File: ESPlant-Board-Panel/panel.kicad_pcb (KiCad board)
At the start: 2 copper layers, 156 x 147 mm, 408 parts, among them J1 Conn_01x05, U1 ESP32-C6-MINI-1/U, U3 Reset, U4 Boot, U5 Temp/Humid-Sensor, U6 Light sensor, U7 AMS1117-3_3, U8 MK-12C02-G025

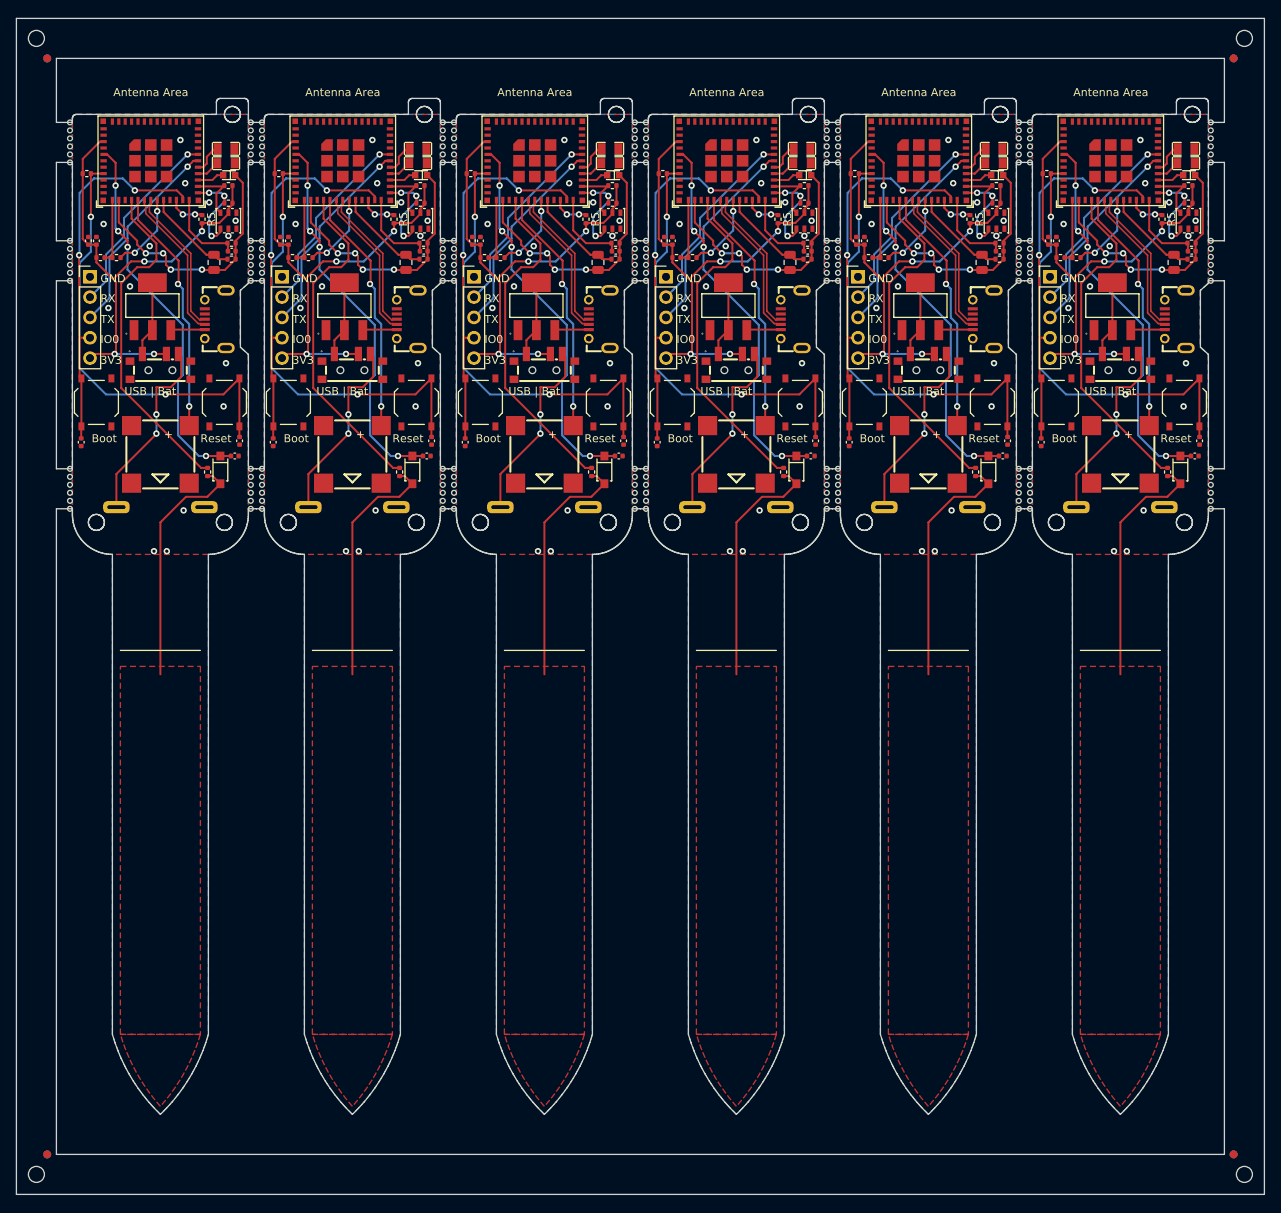
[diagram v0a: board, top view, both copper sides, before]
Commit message: Case: Add v2 case with improved folder structure
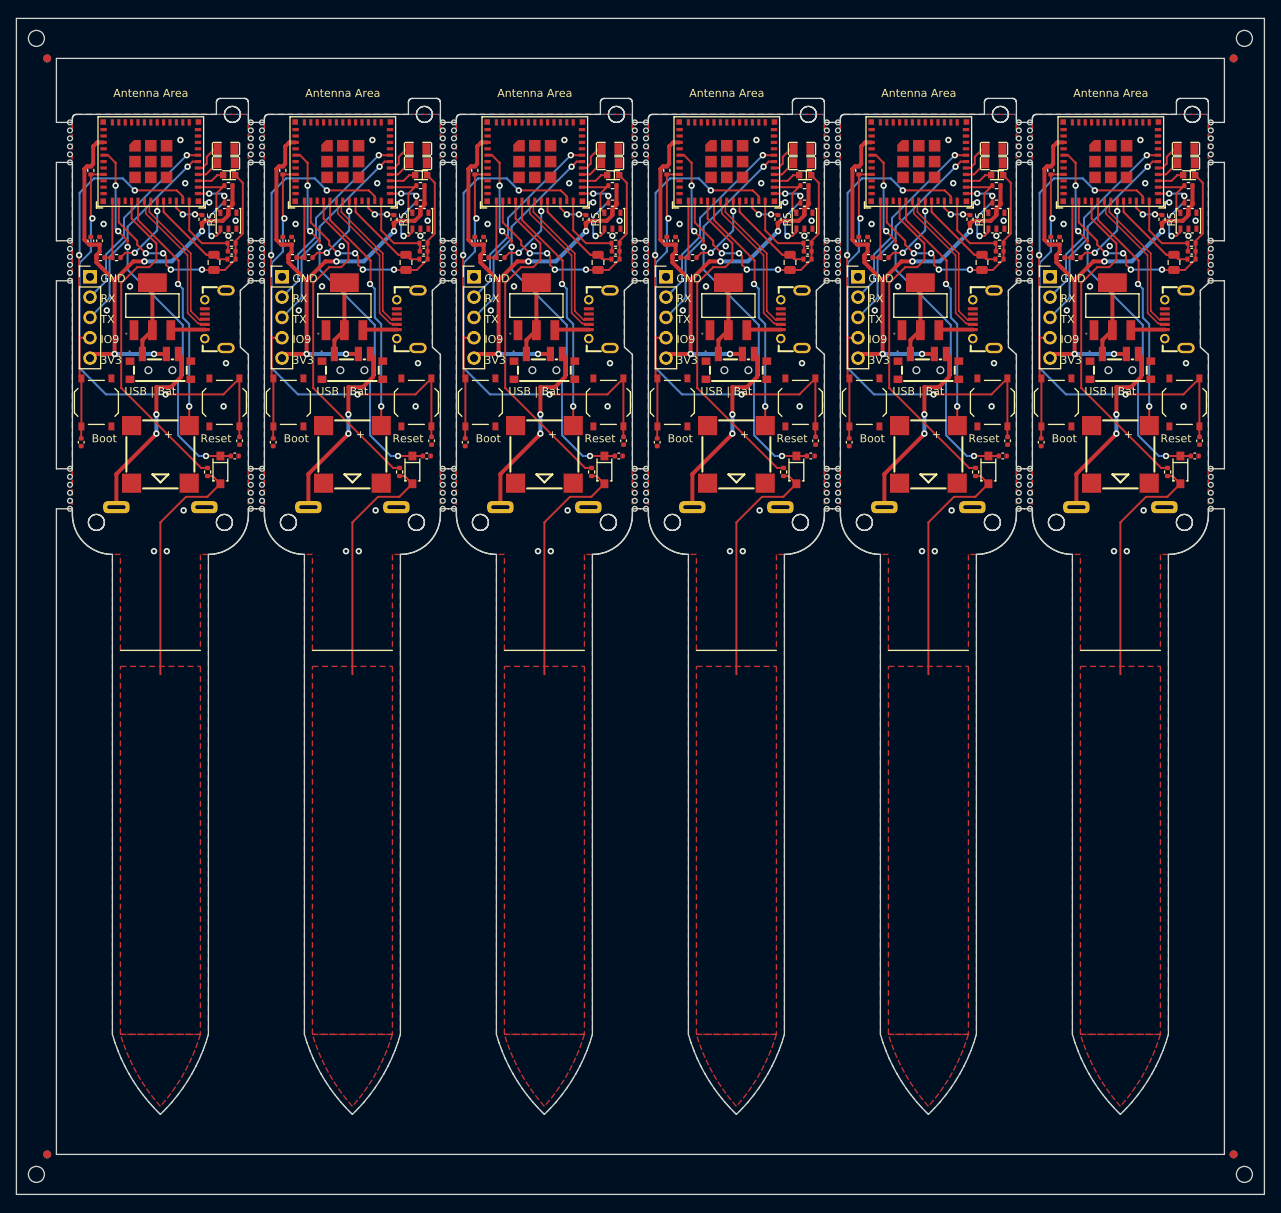
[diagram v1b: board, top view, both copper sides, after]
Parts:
- removed the C8 at (253.0, 47.8)
- removed the C8 at (277.0, 47.8)
- removed the C8 at (229.0, 47.8)
- removed the C8 at (181.0, 47.8)
- removed the C8 at (157.0, 47.8)
- removed the C8 at (205.0, 47.8)
- removed the C9 at (252.0, 47.8)
- removed the C9 at (204.0, 47.8)
- removed the C9 at (180.0, 47.8)
- removed the C9 at (228.0, 47.8)
- removed the C9 at (276.0, 47.8)
- removed the C9 at (156.0, 47.8)
- removed the R9 at (203.8, 39.4)
- removed the R9 at (251.8, 39.4)
- removed the R9 at (179.8, 39.4)
- removed the R9 at (275.8, 39.4)
- removed the R9 at (227.8, 39.4)
- removed the R9 at (155.8, 39.4)
- removed the REF** at (150.9, 162.0) (x2)
- removed the REF** at (299.2, 162.0) (x2)
- removed the REF** at (150.9, 25.0) (x2)
- removed the REF** at (299.2, 25.0) (x2)
- removed the U1 at (259.8, 35.1)
- removed the U1 at (235.8, 35.1)
- removed the U1 at (187.8, 35.1)
- removed the U1 at (283.8, 35.1)
- removed the U1 at (163.8, 35.1)
- removed the U1 at (211.8, 35.1)
- added C8: 10nF, Capacitor_SMD:C_0402_1005Metric, F.Cu at (181.4, 47.8)
- added C8: 10nF, Capacitor_SMD:C_0402_1005Metric, F.Cu at (229.4, 47.8)
- added C8: 10nF, Capacitor_SMD:C_0402_1005Metric, F.Cu at (205.4, 47.8)
- added C8: 10nF, Capacitor_SMD:C_0402_1005Metric, F.Cu at (253.4, 47.8)
- added C8: 10nF, Capacitor_SMD:C_0402_1005Metric, F.Cu at (157.4, 47.8)
- added C8: 10nF, Capacitor_SMD:C_0402_1005Metric, F.Cu at (277.4, 47.8)
- added C9: 10uF, Capacitor_SMD:C_0402_1005Metric, F.Cu at (252.3, 47.8)
- added C9: 10uF, Capacitor_SMD:C_0402_1005Metric, F.Cu at (204.3, 47.8)
- added C9: 10uF, Capacitor_SMD:C_0402_1005Metric, F.Cu at (228.3, 47.8)
- added C9: 10uF, Capacitor_SMD:C_0402_1005Metric, F.Cu at (156.3, 47.8)
- added C9: 10uF, Capacitor_SMD:C_0402_1005Metric, F.Cu at (276.3, 47.8)
- added C9: 10uF, Capacitor_SMD:C_0402_1005Metric, F.Cu at (180.3, 47.8)
- added R9: 10k, Resistor_SMD:R_0402_1005Metric, F.Cu at (180.3, 39.0)
- added R9: 10k, Resistor_SMD:R_0402_1005Metric, F.Cu at (252.3, 39.0)
- added R9: 10k, Resistor_SMD:R_0402_1005Metric, F.Cu at (276.3, 39.0)
- added R9: 10k, Resistor_SMD:R_0402_1005Metric, F.Cu at (204.3, 39.0)
- added R9: 10k, Resistor_SMD:R_0402_1005Metric, F.Cu at (228.3, 39.0)
- added R9: 10k, Resistor_SMD:R_0402_1005Metric, F.Cu at (156.3, 39.0)
- added REF**: Fiducial, Fiducial, F.Cu at (150.9, 25.0)
- added REF**: Fiducial, Fiducial, F.Cu at (150.9, 162.0)
- added REF**: Fiducial, Fiducial, F.Cu at (299.2, 162.0)
- added REF**: Fiducial, Fiducial, F.Cu at (299.2, 25.0)
- added REF**: Fiducial, Fiducial, B.Cu at (150.9, 25.0)
- added REF**: Fiducial, Fiducial, B.Cu at (299.2, 162.0)
- added REF**: Fiducial, Fiducial, B.Cu at (299.2, 25.0)
- added REF**: Fiducial, Fiducial, B.Cu at (150.9, 162.0)
- added U1: ESP32-C6-MINI-1/U, Espressif:ESP32-C6-MINI-1, F.Cu at (211.8, 35.2)
- added U1: ESP32-C6-MINI-1/U, Espressif:ESP32-C6-MINI-1, F.Cu at (235.8, 35.2)
- added U1: ESP32-C6-MINI-1/U, Espressif:ESP32-C6-MINI-1, F.Cu at (259.8, 35.2)
- added U1: ESP32-C6-MINI-1/U, Espressif:ESP32-C6-MINI-1, F.Cu at (283.8, 35.2)
- added U1: ESP32-C6-MINI-1/U, Espressif:ESP32-C6-MINI-1, F.Cu at (187.8, 35.2)
- added U1: ESP32-C6-MINI-1/U, Espressif:ESP32-C6-MINI-1, F.Cu at (163.8, 35.2)
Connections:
- net Board_0-Net-(U7-VOUT-Pad2) renamed Board_0-/USB
- net Board_0-Net-(U9-+) renamed Board_0-/BAT
- net Board_1-Net-(U7-VOUT-Pad2) renamed Board_1-/USB
- net Board_1-Net-(U9-+) renamed Board_1-/BAT
- net Board_2-Net-(U7-VOUT-Pad2) renamed Board_2-/USB
- net Board_2-Net-(U9-+) renamed Board_2-/BAT
- net Board_3-Net-(U7-VOUT-Pad2) renamed Board_3-/USB
- net Board_3-Net-(U9-+) renamed Board_3-/BAT
- net Board_4-Net-(U7-VOUT-Pad2) renamed Board_4-/USB
- net Board_4-Net-(U9-+) renamed Board_4-/BAT
- net Board_5-Net-(U7-VOUT-Pad2) renamed Board_5-/USB
- net Board_5-Net-(U9-+) renamed Board_5-/BAT
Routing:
- net Board_5-+3V3: track 62.1 -> 62.7 mm
- net Board_4-+3V3: track 62.1 -> 62.7 mm
- net Board_3-+3V3: track 62.1 -> 62.7 mm
- net Board_2-+3V3: track 62.1 -> 62.7 mm
- net Board_1-+3V3: track 62.1 -> 62.7 mm
- net Board_0-+3V3: track 62.1 -> 62.7 mm
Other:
- board text added: "IO9"
- board text removed: "IO0"

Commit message: Finish v2.0 for prototyping
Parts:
- removed the BZ1 at (165.0, 74.5)
- removed the BZ1 at (237.0, 74.5)
- removed the BZ1 at (189.0, 74.5)
- removed the BZ1 at (213.0, 74.5)
- removed the BZ1 at (285.0, 74.5)
- removed the BZ1 at (261.0, 74.5)
- removed the C1 at (270.9, 72.8)
- removed the C1 at (198.9, 72.8)
- removed the C1 at (222.9, 72.8)
- removed the C1 at (246.9, 72.8)
- removed the C1 at (294.9, 72.8)
- removed the C1 at (174.9, 72.8)
- removed the C2 at (155.1, 73.0)
- removed the C2 at (251.1, 73.0)
- removed the C2 at (179.1, 73.0)
- removed the C2 at (275.1, 73.0)
- removed the C2 at (227.1, 73.0)
- removed the C2 at (203.1, 73.0)
- removed the C3 at (294.3, 74.7)
- removed the C3 at (222.3, 74.7)
- removed the C3 at (198.3, 74.7)
- removed the C3 at (246.3, 74.7)
- removed the C3 at (174.3, 74.7)
- removed the C3 at (270.3, 74.7)
- removed the C5 at (173.9, 49.1)
- removed the C5 at (269.9, 49.1)
- removed the C5 at (197.9, 49.1)
- removed the C5 at (293.9, 49.1)
- removed the C5 at (221.9, 49.1)
- removed the C5 at (245.9, 49.1)
- removed the C7 at (243.7, 50.5)
- removed the C7 at (219.7, 50.5)
- removed the C7 at (195.7, 50.5)
- removed the C7 at (267.7, 50.5)
- removed the C7 at (171.7, 50.5)
- removed the C7 at (291.7, 50.5)
- removed the C8 at (181.4, 47.8)
- removed the C8 at (229.4, 47.8)
- removed the C8 at (205.4, 47.8)
- removed the C8 at (253.4, 47.8)
- removed the C8 at (157.4, 47.8)
- removed the C8 at (277.4, 47.8)
- removed the C9 at (252.3, 47.8)
- removed the C9 at (204.3, 47.8)
- removed the C9 at (228.3, 47.8)
- removed the C9 at (156.3, 47.8)
- removed the C9 at (276.3, 47.8)
- removed the C9 at (180.3, 47.8)
- removed the D1 at (245.2, 36.3)
- removed the D1 at (293.2, 36.3)
- removed the D1 at (269.2, 36.3)
- removed the D1 at (221.2, 36.3)
- removed the D1 at (173.2, 36.3)
- removed the D1 at (197.2, 36.3)
- removed the D2 at (172.5, 76.4)
- removed the D2 at (220.5, 76.4)
- removed the D2 at (196.5, 76.4)
- removed the D2 at (292.5, 76.4)
- removed the D2 at (268.5, 76.4)
- removed the D2 at (244.5, 76.4)
- removed the D3 at (173.2, 38.1)
- removed the D3 at (197.2, 38.1)
- removed the D3 at (221.2, 38.1)
- removed the D3 at (245.2, 38.1)
- removed the D3 at (269.2, 38.1)
- removed the D3 at (293.2, 38.1)
- removed the J1 at (276.2, 52.3)
- removed the J1 at (204.2, 52.3)
- removed the J1 at (180.2, 52.3)
- removed the J1 at (228.2, 52.3)
- removed the J1 at (252.2, 52.3)
- removed the J1 at (156.2, 52.3)
- removed the R1 at (269.9, 48.1)
- removed the R1 at (173.9, 48.1)
- removed the R1 at (293.9, 48.1)
- removed the R1 at (221.9, 48.1)
- removed the R1 at (245.9, 48.1)
- removed the R1 at (197.9, 48.1)
- removed the R10 at (221.5, 43.1)
- removed the R10 at (245.5, 43.1)
- removed the R10 at (293.5, 43.1)
- removed the R10 at (197.5, 43.1)
- removed the R10 at (173.5, 43.1)
- removed the R10 at (269.5, 43.1)
- removed the R2 at (245.5, 40.9)
- removed the R2 at (221.5, 40.9)
- removed the R2 at (269.5, 40.9)
- removed the R2 at (293.5, 40.9)
- removed the R2 at (173.5, 40.9)
- removed the R2 at (197.5, 40.9)
- removed the R3 at (197.9, 50.1)
- removed the R3 at (173.9, 50.1)
- removed the R3 at (293.9, 50.1)
- removed the R3 at (245.9, 50.1)
- removed the R3 at (221.9, 50.1)
- removed the R3 at (269.9, 50.1)
- removed the R4 at (277.5, 49.9)
- removed the R4 at (205.5, 49.9)
- removed the R4 at (157.5, 49.9)
- removed the R4 at (181.5, 49.9)
- removed the R4 at (253.5, 49.9)
- removed the R4 at (229.5, 49.9)
- removed the R5 at (170.2, 45.1)
- removed the R5 at (266.2, 45.1)
- removed the R5 at (242.2, 45.1)
- removed the R5 at (194.2, 45.1)
- removed the R5 at (290.2, 45.1)
- removed the R5 at (218.2, 45.1)
- removed the R6 at (231.5, 49.9)
- removed the R6 at (183.5, 49.9)
- removed the R6 at (207.5, 49.9)
- removed the R6 at (255.5, 49.9)
- removed the R6 at (279.5, 49.9)
- removed the R6 at (159.5, 49.9)
- removed the R8 at (194.9, 76.7)
- removed the R8 at (266.9, 76.7)
- removed the R8 at (242.9, 76.7)
- removed the R8 at (290.9, 76.7)
- removed the R8 at (218.9, 76.7)
- removed the R8 at (170.9, 76.7)
- removed the R9 at (180.3, 39.0)
- removed the R9 at (252.3, 39.0)
- removed the R9 at (276.3, 39.0)
- removed the R9 at (204.3, 39.0)
- removed the R9 at (228.3, 39.0)
- removed the R9 at (156.3, 39.0)
- removed the REF** at (296.3, 34.0)
- removed the REF** at (224.3, 79.3)
- removed the REF** at (201.7, 50.8)
- removed the REF** at (249.7, 79.3)
- removed the REF** at (201.7, 79.3)
- removed the REF** at (200.3, 80.3)
- removed the REF** at (224.3, 51.8)
- removed the REF** at (153.7, 33.0)
- removed the REF** at (225.7, 50.8)
- removed the REF** at (200.3, 34.0)
- removed the REF** at (201.7, 52.8)
- removed the REF** at (176.3, 35.0)
- removed the REF** at (300.5, 164.5)
- removed the REF** at (201.7, 47.8)
- removed the REF** at (224.3, 50.8)
- removed the REF** at (272.3, 52.8)
- removed the REF** at (248.3, 48.8)
- removed the REF** at (248.3, 50.8)
- removed the REF** at (248.3, 36.0)
- removed the REF** at (176.3, 36.0)
- removed the REF** at (296.3, 52.8)
- removed the REF** at (273.7, 80.3)
- removed the REF** at (153.7, 80.3)
- removed the REF** at (225.7, 38.0)
- removed the REF** at (249.7, 36.0)
- removed the REF** at (177.7, 36.0)
- removed the REF** at (150.9, 25.0) (x2)
- removed the REF** at (177.7, 81.3)
- removed the REF** at (249.7, 48.8)
- removed the REF** at (224.3, 33.0)
- removed the REF** at (153.7, 35.0)
- removed the REF** at (272.3, 35.0)
- removed the REF** at (201.7, 36.0)
- removed the REF** at (225.7, 78.3)
- removed the REF** at (272.3, 38.0)
- removed the REF** at (224.3, 34.0)
- removed the REF** at (153.7, 52.8)
- removed the REF** at (200.3, 77.3)
- removed the REF** at (177.7, 76.3)
- removed the REF** at (201.7, 80.3)
- removed the REF** at (224.3, 35.0)
- removed the REF** at (225.7, 76.3)
- removed the REF** at (225.7, 79.3)
- removed the REF** at (225.7, 77.3)
- removed the REF** at (225.7, 48.8)
- removed the REF** at (150.9, 162.0) (x2)
- removed the REF** at (272.3, 49.8)
- removed the REF** at (296.3, 81.3)
- removed the REF** at (248.3, 79.3)
- removed the REF** at (299.2, 162.0) (x2)
- removed the REF** at (249.7, 34.0)
- removed the REF** at (200.3, 49.8)
- removed the REF** at (273.7, 47.8)
- removed the REF** at (200.3, 38.0)
- removed the REF** at (200.3, 52.8)
- removed the REF** at (272.3, 48.8)
- removed the REF** at (176.3, 79.3)
- removed the REF** at (149.5, 164.5)
- removed the REF** at (273.7, 37.0)
- removed the REF** at (273.7, 81.3)
- removed the REF** at (225.7, 34.0)
- removed the REF** at (248.3, 78.3)
- removed the REF** at (249.7, 37.0)
- removed the REF** at (153.7, 76.3)
- removed the REF** at (201.7, 35.0)
- removed the REF** at (153.7, 47.8)
- removed the REF** at (296.3, 38.0)
- removed the REF** at (296.3, 78.3)
- removed the REF** at (176.3, 33.0)
- removed the REF** at (176.3, 37.0)
- removed the REF** at (248.3, 49.8)
- removed the REF** at (249.7, 50.8)
- removed the REF** at (272.3, 76.3)
- removed the REF** at (200.3, 36.0)
- removed the REF** at (273.7, 33.0)
- removed the REF** at (273.7, 78.3)
- removed the REF** at (248.3, 81.3)
- removed the REF** at (248.3, 35.0)
- removed the REF** at (224.3, 49.8)
- removed the REF** at (225.7, 36.0)
- removed the REF** at (296.3, 47.8)
- removed the REF** at (153.7, 81.3)
- removed the REF** at (176.3, 38.0)
- removed the REF** at (177.7, 34.0)
- removed the REF** at (249.7, 47.8)
- removed the REF** at (225.7, 47.8)
- removed the REF** at (153.7, 34.0)
- removed the REF** at (177.7, 37.0)
- removed the REF** at (200.3, 48.8)
- removed the REF** at (225.7, 52.8)
- removed the REF** at (296.3, 49.8)
- removed the REF** at (248.3, 37.0)
- removed the REF** at (296.3, 76.3)
- removed the REF** at (273.7, 35.0)
- removed the REF** at (201.7, 38.0)
- removed the REF** at (201.7, 48.8)
- removed the REF** at (248.3, 38.0)
- removed the REF** at (176.3, 77.3)
- removed the REF** at (224.3, 78.3)
- removed the REF** at (177.7, 35.0)
- removed the REF** at (224.3, 47.8)
- removed the REF** at (176.3, 51.8)
- removed the REF** at (273.7, 52.8)
- removed the REF** at (153.7, 50.8)
- removed the REF** at (248.3, 47.8)
- removed the REF** at (201.7, 51.8)
- removed the REF** at (272.3, 80.3)
- removed the REF** at (153.7, 48.8)
- removed the REF** at (153.7, 38.0)
- removed the REF** at (299.2, 25.0) (x2)
- removed the REF** at (296.3, 80.3)
- removed the REF** at (225.7, 33.0)
- removed the REF** at (273.7, 34.0)
- removed the REF** at (177.7, 50.8)
- removed the REF** at (176.3, 50.8)
- removed the REF** at (273.7, 36.0)
- removed the REF** at (153.7, 36.0)
- removed the REF** at (249.7, 80.3)
- removed the REF** at (176.3, 48.8)
- removed the REF** at (200.3, 76.3)
- removed the REF** at (273.7, 79.3)
- removed the REF** at (248.3, 80.3)
- removed the REF** at (153.7, 79.3)
- removed the REF** at (176.3, 78.3)
- removed the REF** at (296.3, 77.3)
- removed the REF** at (249.7, 76.3)
- removed the REF** at (177.7, 47.8)
- removed the REF** at (177.7, 33.0)
- removed the REF** at (224.3, 37.0)
- removed the REF** at (248.3, 33.0)
- removed the REF** at (200.3, 78.3)
- removed the REF** at (272.3, 81.3)
- removed the REF** at (296.3, 50.8)
- removed the REF** at (153.7, 37.0)
- removed the REF** at (225.7, 49.8)
- removed the REF** at (248.3, 34.0)
- removed the REF** at (225.7, 51.8)
- removed the REF** at (272.3, 77.3)
- removed the REF** at (248.3, 52.8)
- removed the REF** at (201.7, 76.3)
- removed the REF** at (177.7, 80.3)
- removed the REF** at (201.7, 81.3)
- removed the REF** at (153.7, 51.8)
- removed the REF** at (296.3, 48.8)
- removed the REF** at (149.5, 22.5)
- removed the REF** at (177.7, 49.8)
- removed the REF** at (200.3, 35.0)
- removed the REF** at (273.7, 76.3)
- removed the REF** at (201.7, 49.8)
- removed the REF** at (249.7, 77.3)
- removed the REF** at (272.3, 37.0)
- removed the REF** at (249.7, 35.0)
- removed the REF** at (248.3, 77.3)
- removed the REF** at (201.7, 37.0)
- removed the REF** at (273.7, 50.8)
- removed the REF** at (177.7, 52.8)
- removed the REF** at (249.7, 78.3)
- removed the REF** at (296.3, 79.3)
- removed the REF** at (224.3, 36.0)
- removed the REF** at (153.7, 78.3)
- removed the REF** at (296.3, 51.8)
- removed the REF** at (249.7, 49.8)
- removed the REF** at (200.3, 79.3)
- removed the REF** at (176.3, 34.0)
- removed the REF** at (201.7, 33.0)
- removed the REF** at (248.3, 51.8)
- removed the REF** at (224.3, 48.8)
- removed the REF** at (272.3, 51.8)
- removed the REF** at (296.3, 33.0)
- removed the REF** at (177.7, 77.3)
- removed the REF** at (272.3, 78.3)
- removed the REF** at (200.3, 33.0)
- removed the REF** at (300.5, 22.5)
- removed the REF** at (176.3, 81.3)
- removed the REF** at (225.7, 35.0)
- removed the REF** at (225.7, 80.3)
- removed the REF** at (224.3, 81.3)
- removed the REF** at (224.3, 77.3)
- removed the REF** at (153.7, 77.3)
- removed the REF** at (177.7, 78.3)
- removed the REF** at (177.7, 51.8)
- removed the REF** at (272.3, 36.0)
- removed the REF** at (249.7, 38.0)
- removed the REF** at (225.7, 37.0)
- removed the REF** at (200.3, 81.3)
- removed the REF** at (296.3, 35.0)
- removed the REF** at (200.3, 51.8)
- removed the REF** at (176.3, 80.3)
- removed the REF** at (201.7, 34.0)
- removed the REF** at (249.7, 81.3)
- removed the REF** at (272.3, 33.0)
- removed the REF** at (272.3, 79.3)
- removed the REF** at (273.7, 77.3)
- removed the REF** at (272.3, 34.0)
- removed the REF** at (224.3, 76.3)
- removed the REF** at (176.3, 76.3)
- removed the REF** at (201.7, 77.3)
- removed the REF** at (176.3, 47.8)
- removed the REF** at (272.3, 47.8)
- removed the REF** at (224.3, 80.3)
- removed the REF** at (177.7, 38.0)
- removed the REF** at (249.7, 52.8)
- removed the REF** at (177.7, 79.3)
- removed the REF** at (200.3, 47.8)
- removed the REF** at (224.3, 38.0)
- removed the REF** at (273.7, 38.0)
- removed the REF** at (249.7, 33.0)
- removed the REF** at (296.3, 37.0)
- removed the REF** at (224.3, 52.8)
- removed the REF** at (273.7, 49.8)
- removed the REF** at (200.3, 50.8)
- removed the REF** at (177.7, 48.8)
- removed the REF** at (176.3, 52.8)
- removed the REF** at (200.3, 37.0)
- removed the REF** at (273.7, 51.8)
- removed the REF** at (225.7, 81.3)
- removed the REF** at (201.7, 78.3)
- removed the REF** at (273.7, 48.8)
- removed the REF** at (176.3, 49.8)
- removed the REF** at (296.3, 36.0)
- removed the REF** at (153.7, 49.8)
- removed the REF** at (272.3, 50.8)
- removed the REF** at (249.7, 51.8)
- removed the REF** at (248.3, 76.3)
- removed the U1 at (211.8, 35.2)
- removed the U1 at (235.8, 35.2)
- removed the U1 at (259.8, 35.2)
- removed the U1 at (283.8, 35.2)
- removed the U1 at (187.8, 35.2)
- removed the U1 at (163.8, 35.2)
- removed the U3 at (269.0, 68.0)
- removed the U3 at (221.0, 68.0)
- removed the U3 at (245.0, 68.0)
- removed the U3 at (293.0, 68.0)
- removed the U3 at (173.0, 68.0)
- removed the U3 at (197.0, 68.0)
- removed the U4 at (181.0, 68.0)
- removed the U4 at (229.0, 68.0)
- removed the U4 at (277.0, 68.0)
- removed the U4 at (205.0, 68.0)
- removed the U4 at (157.0, 68.0)
- removed the U4 at (253.0, 68.0)
- removed the U5 at (269.5, 45.3)
- removed the U5 at (293.5, 45.3)
- removed the U5 at (173.5, 45.3)
- removed the U5 at (221.5, 45.3)
- removed the U5 at (245.5, 45.3)
- removed the U5 at (197.5, 45.3)
- removed the U6 at (245.6, 39.6)
- removed the U6 at (221.6, 39.6)
- removed the U6 at (173.6, 39.6)
- removed the U6 at (293.6, 39.6)
- removed the U6 at (269.6, 39.6)
- removed the U6 at (197.6, 39.6)
- removed the U7 at (188.0, 56.0)
- removed the U7 at (164.0, 56.0)
- removed the U7 at (236.0, 56.0)
- removed the U7 at (212.0, 56.0)
- removed the U7 at (260.0, 56.0)
- removed the U7 at (284.0, 56.0)
- removed the U8 at (285.0, 63.5)
- removed the U8 at (237.0, 63.5)
- removed the U8 at (261.0, 63.5)
- removed the U8 at (165.0, 63.5)
- removed the U8 at (213.0, 63.5)
- removed the U8 at (189.0, 63.5)
- removed the U9 at (165.0, 81.1)
- removed the U9 at (285.0, 81.1)
- removed the U9 at (213.0, 81.1)
- removed the U9 at (261.0, 81.1)
- removed the U9 at (189.0, 81.1)
- removed the U9 at (237.0, 81.1)
- removed the USB1 at (195.9, 57.6)
- removed the USB1 at (267.9, 57.6)
- removed the USB1 at (219.9, 57.6)
- removed the USB1 at (171.9, 57.6)
- removed the USB1 at (243.9, 57.6)
- removed the USB1 at (291.9, 57.6)
- added BZ1: Buzzer, CustomFootprints:BUZ-SMD_4P-L8.5-W8.5-P8.50-BR, F.Cu at (249.0, 74.5)
- added BZ1: Buzzer, CustomFootprints:BUZ-SMD_4P-L8.5-W8.5-P8.50-BR, F.Cu at (201.0, 74.5)
- added BZ1: Buzzer, CustomFootprints:BUZ-SMD_4P-L8.5-W8.5-P8.50-BR, F.Cu at (177.0, 74.5)
- added BZ1: Buzzer, CustomFootprints:BUZ-SMD_4P-L8.5-W8.5-P8.50-BR, F.Cu at (273.0, 74.5)
- added BZ1: Buzzer, CustomFootprints:BUZ-SMD_4P-L8.5-W8.5-P8.50-BR, F.Cu at (225.0, 74.5)
- added C1: 100nF, Capacitor_SMD:C_0402_1005Metric, F.Cu at (186.9, 72.8)
- added C1: 100nF, Capacitor_SMD:C_0402_1005Metric, F.Cu at (210.9, 72.8)
- added C1: 100nF, Capacitor_SMD:C_0402_1005Metric, F.Cu at (258.9, 72.8)
- added C1: 100nF, Capacitor_SMD:C_0402_1005Metric, F.Cu at (234.9, 72.8)
- added C1: 100nF, Capacitor_SMD:C_0402_1005Metric, F.Cu at (282.9, 72.8)
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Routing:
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- removed copper zone on F.Cu, net Board_5-/SensorCapV
- removed copper zone on B.Cu, net Board_5-GND
- removed copper zone on F.Cu, net Board_5-GND
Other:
- board size 156 x 147 mm -> 132 x 147 mm

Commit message: Board: Update panel
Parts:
- removed the BZ1 at (249.0, 74.5)
- removed the BZ1 at (201.0, 74.5)
- removed the BZ1 at (177.0, 74.5)
- removed the BZ1 at (273.0, 74.5)
- removed the BZ1 at (225.0, 74.5)
- removed the C1 at (186.9, 72.8)
- removed the C1 at (210.9, 72.8)
- removed the C1 at (258.9, 72.8)
- removed the C1 at (234.9, 72.8)
- removed the C1 at (282.9, 72.8)
- removed the C2 at (263.1, 73.0)
- removed the C2 at (239.1, 73.0)
- removed the C2 at (215.1, 73.0)
- removed the C2 at (167.1, 73.0)
- removed the C2 at (191.1, 73.0)
- removed the C3 at (210.3, 74.7)
- removed the C3 at (258.3, 74.7)
- removed the C3 at (186.3, 74.7)
- removed the C3 at (234.3, 74.7)
- removed the C3 at (282.3, 74.7)
- removed the C5 at (185.9, 49.1)
- removed the C5 at (257.9, 49.1)
- removed the C5 at (281.9, 49.1)
- removed the C5 at (233.9, 49.1)
- removed the C5 at (209.9, 49.1)
- removed the C7 at (231.7, 50.5)
- removed the C7 at (255.7, 50.5)
- removed the C7 at (183.7, 50.5)
- removed the C7 at (279.7, 50.5)
- removed the C7 at (207.7, 50.5)
- removed the C8 at (193.4, 47.8)
- removed the C8 at (241.4, 47.8)
- removed the C8 at (265.4, 47.8)
- removed the C8 at (217.4, 47.8)
- removed the C8 at (169.4, 47.8)
- removed the C9 at (168.3, 47.8)
- removed the C9 at (264.3, 47.8)
- removed the C9 at (216.3, 47.8)
- removed the C9 at (192.3, 47.8)
- removed the C9 at (240.3, 47.8)
- removed the D1 at (281.2, 36.3)
- removed the D1 at (233.2, 36.3)
- removed the D1 at (209.2, 36.3)
- removed the D1 at (185.2, 36.3)
- removed the D1 at (257.2, 36.3)
- removed the D2 at (232.5, 76.4)
- removed the D2 at (184.5, 76.4)
- removed the D2 at (280.5, 76.4)
- removed the D2 at (256.5, 76.4)
- removed the D2 at (208.5, 76.4)
- removed the D3 at (257.2, 38.1)
- removed the D3 at (209.2, 38.1)
- removed the D3 at (281.2, 38.1)
- removed the D3 at (233.2, 38.1)
- removed the D3 at (185.2, 38.1)
- removed the J1 at (168.2, 52.3)
- removed the J1 at (216.2, 52.3)
- removed the J1 at (264.2, 52.3)
- removed the J1 at (240.2, 52.3)
- removed the J1 at (192.2, 52.3)
- removed the R1 at (185.9, 48.1)
- removed the R1 at (209.9, 48.1)
- removed the R1 at (281.9, 48.1)
- removed the R1 at (257.9, 48.1)
- removed the R1 at (233.9, 48.1)
- removed the R10 at (209.5, 43.1)
- removed the R10 at (257.5, 43.1)
- removed the R10 at (233.5, 43.1)
- removed the R10 at (281.5, 43.1)
- removed the R10 at (185.5, 43.1)
- removed the R2 at (281.5, 40.9)
- removed the R2 at (257.5, 40.9)
- removed the R2 at (209.5, 40.9)
- removed the R2 at (185.5, 40.9)
- removed the R2 at (233.5, 40.9)
- removed the R3 at (185.9, 50.1)
- removed the R3 at (257.9, 50.1)
- removed the R3 at (233.9, 50.1)
- removed the R3 at (209.9, 50.1)
- removed the R3 at (281.9, 50.1)
- removed the R4 at (193.5, 49.9)
- removed the R4 at (169.5, 49.9)
- removed the R4 at (241.5, 49.9)
- removed the R4 at (265.5, 49.9)
- removed the R4 at (217.5, 49.9)
- removed the R5 at (278.2, 45.1)
- removed the R5 at (254.2, 45.1)
- removed the R5 at (230.2, 45.1)
- removed the R5 at (206.2, 45.1)
- removed the R5 at (182.2, 45.1)
- removed the R6 at (195.5, 49.9)
- removed the R6 at (219.5, 49.9)
- removed the R6 at (171.5, 49.9)
- removed the R6 at (267.5, 49.9)
- removed the R6 at (243.5, 49.9)
- removed the R8 at (254.9, 76.7)
- removed the R8 at (206.9, 76.7)
- removed the R8 at (182.9, 76.7)
- removed the R8 at (278.9, 76.7)
- removed the R8 at (230.9, 76.7)
- removed the R9 at (264.3, 39.0)
- removed the R9 at (216.3, 39.0)
- removed the R9 at (192.3, 39.0)
- removed the R9 at (168.3, 39.0)
- removed the R9 at (240.3, 39.0)
- removed the REF** at (260.3, 81.0)
- removed the REF** at (188.3, 51.5)
- removed the REF** at (236.3, 48.5)
- removed the REF** at (260.3, 52.5)
- removed the REF** at (213.7, 50.5)
- removed the REF** at (236.3, 37.4)
- removed the REF** at (260.3, 76.0)
- removed the REF** at (165.7, 37.4)
- removed the REF** at (260.3, 49.5)
- removed the REF** at (284.3, 77.0)
- removed the REF** at (260.3, 80.0)
- removed the REF** at (161.5, 22.5)
- removed the REF** at (288.5, 164.5)
- removed the REF** at (212.3, 48.5)
- removed the REF** at (260.3, 36.4)
- removed the REF** at (261.7, 79.0)
- removed the REF** at (237.7, 50.5)
- removed the REF** at (236.3, 33.4)
- removed the REF** at (260.3, 35.4)
- removed the REF** at (261.7, 33.4)
- removed the REF** at (237.7, 47.5)
- removed the REF** at (212.3, 52.5)
- removed the REF** at (165.7, 35.4)
- removed the REF** at (261.7, 77.0)
- removed the REF** at (188.3, 34.4)
- removed the REF** at (212.3, 49.5)
- removed the REF** at (260.3, 77.0)
- removed the REF** at (189.7, 34.4)
- removed the REF** at (261.7, 80.0)
- removed the REF** at (189.7, 78.0)
- removed the REF** at (213.7, 52.5)
- removed the REF** at (260.3, 37.4)
- removed the REF** at (260.3, 47.5)
- removed the REF** at (189.7, 48.5)
- removed the REF** at (189.7, 76.0)
- removed the REF** at (236.3, 78.0)
- removed the REF** at (165.7, 51.5)
- removed the REF** at (188.3, 33.4)
- removed the REF** at (261.7, 37.4)
- removed the REF** at (261.7, 36.4)
- removed the REF** at (189.7, 35.4)
- removed the REF** at (237.7, 51.5)
- removed the REF** at (236.3, 47.5)
- removed the REF** at (261.7, 78.0)
- removed the REF** at (284.3, 79.0)
- removed the REF** at (236.3, 36.4)
- removed the REF** at (236.3, 81.0)
- removed the REF** at (236.3, 50.5)
- removed the REF** at (236.3, 79.0)
- removed the REF** at (165.7, 78.0)
- removed the REF** at (213.7, 51.5)
- removed the REF** at (261.7, 47.5)
- removed the REF** at (236.3, 52.5)
- removed the REF** at (261.7, 38.4)
- removed the REF** at (189.7, 33.4)
- removed the REF** at (213.7, 37.4)
- removed the REF** at (189.7, 37.4)
- removed the REF** at (188.3, 80.0)
- removed the REF** at (236.3, 77.0)
- removed the REF** at (213.7, 81.0)
- removed the REF** at (213.7, 36.4)
- removed the REF** at (261.7, 51.5)
- removed the REF** at (212.3, 38.4)
- removed the REF** at (237.7, 34.4)
- removed the REF** at (236.3, 38.4)
- removed the REF** at (261.7, 81.0)
- removed the REF** at (188.3, 52.5)
- removed the REF** at (237.7, 48.5)
- removed the REF** at (189.7, 52.5)
- removed the REF** at (165.7, 36.4)
- removed the REF** at (165.7, 52.5)
- removed the REF** at (237.7, 49.5)
- removed the REF** at (189.7, 79.0)
- removed the REF** at (165.7, 48.5)
- removed the REF** at (261.7, 49.5)
- removed the REF** at (188.3, 38.4)
- removed the REF** at (188.3, 49.5)
- removed the REF** at (213.7, 78.0)
- removed the REF** at (284.3, 36.4)
- removed the REF** at (162.9, 162.0) (x2)
- removed the REF** at (212.3, 37.4)
- removed the REF** at (284.3, 49.5)
- removed the REF** at (165.7, 50.5)
- removed the REF** at (237.7, 79.0)
- removed the REF** at (161.5, 164.5)
- removed the REF** at (284.3, 50.5)
- removed the REF** at (260.3, 51.5)
- removed the REF** at (284.3, 38.4)
- removed the REF** at (165.7, 79.0)
- removed the REF** at (261.7, 50.5)
- removed the REF** at (189.7, 49.5)
- removed the REF** at (189.7, 77.0)
- removed the REF** at (212.3, 50.5)
- removed the REF** at (165.7, 34.4)
- removed the REF** at (213.7, 49.5)
- removed the REF** at (213.7, 80.0)
- removed the REF** at (165.7, 76.0)
- removed the REF** at (189.7, 80.0)
- removed the REF** at (212.3, 36.4)
- removed the REF** at (287.2, 162.0) (x2)
- removed the REF** at (189.7, 50.5)
- removed the REF** at (287.2, 25.0) (x2)
- removed the REF** at (162.9, 25.0) (x2)
- removed the REF** at (188.3, 37.4)
- removed the REF** at (260.3, 50.5)
- removed the REF** at (288.5, 22.5)
- removed the REF** at (260.3, 38.4)
- removed the REF** at (212.3, 81.0)
- removed the REF** at (237.7, 38.4)
- removed the REF** at (284.3, 37.4)
- removed the REF** at (188.3, 81.0)
- removed the REF** at (165.7, 77.0)
- removed the REF** at (237.7, 76.0)
- removed the REF** at (284.3, 78.0)
- removed the REF** at (261.7, 52.5)
- removed the REF** at (212.3, 33.4)
- removed the REF** at (189.7, 47.5)
- removed the REF** at (165.7, 80.0)
- removed the REF** at (260.3, 48.5)
- removed the REF** at (284.3, 48.5)
- removed the REF** at (213.7, 34.4)
- removed the REF** at (284.3, 35.4)
- removed the REF** at (284.3, 81.0)
- removed the REF** at (165.7, 47.5)
- removed the REF** at (261.7, 34.4)
- removed the REF** at (236.3, 35.4)
- removed the REF** at (236.3, 76.0)
- removed the REF** at (237.7, 77.0)
- removed the REF** at (189.7, 51.5)
- removed the REF** at (261.7, 35.4)
- removed the REF** at (189.7, 81.0)
- removed the REF** at (213.7, 77.0)
- removed the REF** at (212.3, 79.0)
- removed the REF** at (237.7, 81.0)
- removed the REF** at (236.3, 49.5)
- removed the REF** at (188.3, 36.4)
- removed the REF** at (188.3, 35.4)
- removed the REF** at (284.3, 80.0)
- removed the REF** at (237.7, 78.0)
- removed the REF** at (188.3, 78.0)
- removed the REF** at (188.3, 77.0)
- removed the REF** at (213.7, 35.4)
- removed the REF** at (236.3, 51.5)
- removed the REF** at (261.7, 76.0)
- removed the REF** at (213.7, 79.0)
- removed the REF** at (212.3, 77.0)
- removed the REF** at (237.7, 35.4)
- removed the REF** at (237.7, 33.4)
- removed the REF** at (261.7, 48.5)
- removed the REF** at (284.3, 33.4)
- removed the REF** at (212.3, 47.5)
- removed the REF** at (165.7, 49.5)
- removed the REF** at (212.3, 78.0)
- removed the REF** at (260.3, 78.0)
- removed the REF** at (188.3, 79.0)
- removed the REF** at (260.3, 79.0)
- removed the REF** at (236.3, 34.4)
- removed the REF** at (236.3, 80.0)
- removed the REF** at (212.3, 35.4)
- removed the REF** at (189.7, 36.4)
- removed the REF** at (237.7, 52.5)
- removed the REF** at (284.3, 76.0)
- removed the REF** at (213.7, 47.5)
- removed the REF** at (212.3, 76.0)
- removed the REF** at (212.3, 80.0)
- removed the REF** at (284.3, 52.5)
- removed the REF** at (165.7, 33.4)
- removed the REF** at (284.3, 51.5)
- removed the REF** at (260.3, 33.4)
- removed the REF** at (165.7, 38.4)
- removed the REF** at (284.3, 47.5)
- removed the REF** at (188.3, 48.5)
- removed the REF** at (188.3, 76.0)
- removed the REF** at (237.7, 36.4)
- removed the REF** at (212.3, 34.4)
- removed the REF** at (213.7, 48.5)
- removed the REF** at (213.7, 38.4)
- removed the REF** at (188.3, 47.5)
- removed the REF** at (189.7, 38.4)
- removed the REF** at (165.7, 81.0)
- removed the REF** at (237.7, 80.0)
- removed the REF** at (213.7, 76.0)
- removed the REF** at (284.3, 34.4)
- removed the REF** at (188.3, 50.5)
- removed the REF** at (212.3, 51.5)
- removed the REF** at (237.7, 37.4)
- removed the REF** at (213.7, 33.4)
- removed the REF** at (260.3, 34.4)
- removed the U1 at (199.8, 35.2)
- removed the U1 at (247.8, 35.2)
- removed the U1 at (223.8, 35.2)
- removed the U1 at (175.8, 35.2)
- removed the U1 at (271.8, 35.2)
- removed the U3 at (185.0, 68.0)
- removed the U3 at (281.0, 68.0)
- removed the U3 at (209.0, 68.0)
- removed the U3 at (233.0, 68.0)
- removed the U3 at (257.0, 68.0)
- removed the U4 at (265.0, 68.0)
- removed the U4 at (169.0, 68.0)
- removed the U4 at (193.0, 68.0)
- removed the U4 at (217.0, 68.0)
- removed the U4 at (241.0, 68.0)
- removed the U5 at (257.5, 45.3)
- removed the U5 at (281.5, 45.3)
- removed the U5 at (233.5, 45.3)
- removed the U5 at (209.5, 45.3)
- removed the U5 at (185.5, 45.3)
- removed the U6 at (281.6, 39.6)
- removed the U6 at (209.6, 39.6)
- removed the U6 at (233.6, 39.6)
- removed the U6 at (257.6, 39.6)
- removed the U6 at (185.6, 39.6)
- removed the U7 at (200.0, 56.0)
- removed the U7 at (272.0, 56.0)
- removed the U7 at (248.0, 56.0)
- removed the U7 at (176.0, 56.0)
- removed the U7 at (224.0, 56.0)
- removed the U8 at (201.0, 63.5)
- removed the U8 at (273.0, 63.5)
- removed the U8 at (177.0, 63.5)
- removed the U8 at (225.0, 63.5)
- removed the U8 at (249.0, 63.5)
- removed the U9 at (273.0, 81.1)
- removed the U9 at (177.0, 81.1)
- removed the U9 at (249.0, 81.1)
- removed the U9 at (225.0, 81.1)
- removed the U9 at (201.0, 81.1)
- removed the USB1 at (183.9, 57.6)
- removed the USB1 at (231.9, 57.6)
- removed the USB1 at (255.9, 57.6)
- removed the USB1 at (207.9, 57.6)
- removed the USB1 at (279.9, 57.6)
- added BZ1: Buzzer, CustomFootprints:BUZ-SMD_4P-L8.5-W8.5-P8.50-BR, F.Cu at (285.0, 74.5)
- added BZ1: Buzzer, CustomFootprints:BUZ-SMD_4P-L8.5-W8.5-P8.50-BR, F.Cu at (213.0, 74.5)
- added BZ1: Buzzer, CustomFootprints:BUZ-SMD_4P-L8.5-W8.5-P8.50-BR, F.Cu at (237.0, 74.5)
- added BZ1: Buzzer, CustomFootprints:BUZ-SMD_4P-L8.5-W8.5-P8.50-BR, F.Cu at (189.0, 74.5)
- added BZ1: Buzzer, CustomFootprints:BUZ-SMD_4P-L8.5-W8.5-P8.50-BR, F.Cu at (165.0, 74.5)
- added BZ1: Buzzer, CustomFootprints:BUZ-SMD_4P-L8.5-W8.5-P8.50-BR, F.Cu at (261.0, 74.5)
- added C1: 100nF, Capacitor_SMD:C_0402_1005Metric, F.Cu at (197.0, 72.4)
- added C1: 100nF, Capacitor_SMD:C_0402_1005Metric, F.Cu at (293.0, 72.4)
- added C1: 100nF, Capacitor_SMD:C_0402_1005Metric, F.Cu at (221.0, 72.4)
- added C1: 100nF, Capacitor_SMD:C_0402_1005Metric, F.Cu at (173.0, 72.4)
- added C1: 100nF, Capacitor_SMD:C_0402_1005Metric, F.Cu at (269.0, 72.4)
- added C1: 100nF, Capacitor_SMD:C_0402_1005Metric, F.Cu at (245.0, 72.4)
- added C2: 100nF, Capacitor_SMD:C_0402_1005Metric, F.Cu at (204.9, 72.5)
- added C2: 100nF, Capacitor_SMD:C_0402_1005Metric, F.Cu at (276.9, 72.5)
- added C2: 100nF, Capacitor_SMD:C_0402_1005Metric, F.Cu at (252.9, 72.5)
- added C2: 100nF, Capacitor_SMD:C_0402_1005Metric, F.Cu at (228.9, 72.5)
- added C2: 100nF, Capacitor_SMD:C_0402_1005Metric, F.Cu at (180.9, 72.5)
- added C2: 100nF, Capacitor_SMD:C_0402_1005Metric, F.Cu at (156.9, 72.5)
- added C3: 150pF, Capacitor_SMD:C_0402_1005Metric, F.Cu at (267.1, 72.9)
- added C3: 150pF, Capacitor_SMD:C_0402_1005Metric, F.Cu at (291.1, 72.9)
- added C3: 150pF, Capacitor_SMD:C_0402_1005Metric, F.Cu at (243.1, 72.9)
- added C3: 150pF, Capacitor_SMD:C_0402_1005Metric, F.Cu at (219.1, 72.9)
- added C3: 150pF, Capacitor_SMD:C_0402_1005Metric, F.Cu at (195.1, 72.9)
- added C3: 150pF, Capacitor_SMD:C_0402_1005Metric, F.Cu at (171.1, 72.9)
- added C5: 100nF, Capacitor_SMD:C_0402_1005Metric, F.Cu at (269.9, 49.1)
- added C5: 100nF, Capacitor_SMD:C_0402_1005Metric, F.Cu at (293.9, 49.1)
- added C5: 100nF, Capacitor_SMD:C_0402_1005Metric, F.Cu at (197.9, 49.1)
- added C5: 100nF, Capacitor_SMD:C_0402_1005Metric, F.Cu at (173.9, 49.1)
- added C5: 100nF, Capacitor_SMD:C_0402_1005Metric, F.Cu at (221.9, 49.1)
- added C5: 100nF, Capacitor_SMD:C_0402_1005Metric, F.Cu at (245.9, 49.1)
- added C7: 47uF, Capacitor_SMD:C_0805_2012Metric, F.Cu at (171.7, 50.5)
- added C7: 47uF, Capacitor_SMD:C_0805_2012Metric, F.Cu at (219.7, 50.5)
- added C7: 47uF, Capacitor_SMD:C_0805_2012Metric, F.Cu at (243.7, 50.5)
- added C7: 47uF, Capacitor_SMD:C_0805_2012Metric, F.Cu at (291.7, 50.5)
- added C7: 47uF, Capacitor_SMD:C_0805_2012Metric, F.Cu at (195.7, 50.5)
- added C7: 47uF, Capacitor_SMD:C_0805_2012Metric, F.Cu at (267.7, 50.5)
- added C8: 10nF, Capacitor_SMD:C_0402_1005Metric, F.Cu at (229.4, 47.8)
- added C8: 10nF, Capacitor_SMD:C_0402_1005Metric, F.Cu at (277.4, 47.8)
- added C8: 10nF, Capacitor_SMD:C_0402_1005Metric, F.Cu at (181.4, 47.8)
- added C8: 10nF, Capacitor_SMD:C_0402_1005Metric, F.Cu at (253.4, 47.8)
- added C8: 10nF, Capacitor_SMD:C_0402_1005Metric, F.Cu at (157.4, 47.8)
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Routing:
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- added copper zone on F.Cu, net Board_5-/SensorCapV
- added copper zone on B.Cu, net Board_5-GND
- added copper zone on F.Cu, net Board_5-GND
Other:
- board size 132 x 147 mm -> 156 x 147 mm
- board text removed: "+"
- board text removed: "-"
